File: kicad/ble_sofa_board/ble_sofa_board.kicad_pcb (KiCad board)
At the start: 2 copper layers, 21 parts, among them J1 Screw_Terminal_01x02 VIN, J2 Screw_Terminal_01x02 VOUT, J3 Conn_01x04, J5 Screw_Terminal_01x02 RelayUp, J6 Screw_Terminal_01x02 RelayDwn, J7 RJ9, U1 LM2596S_Buck_Module, U3 Pico_Dual_Channel_Relay_HAT

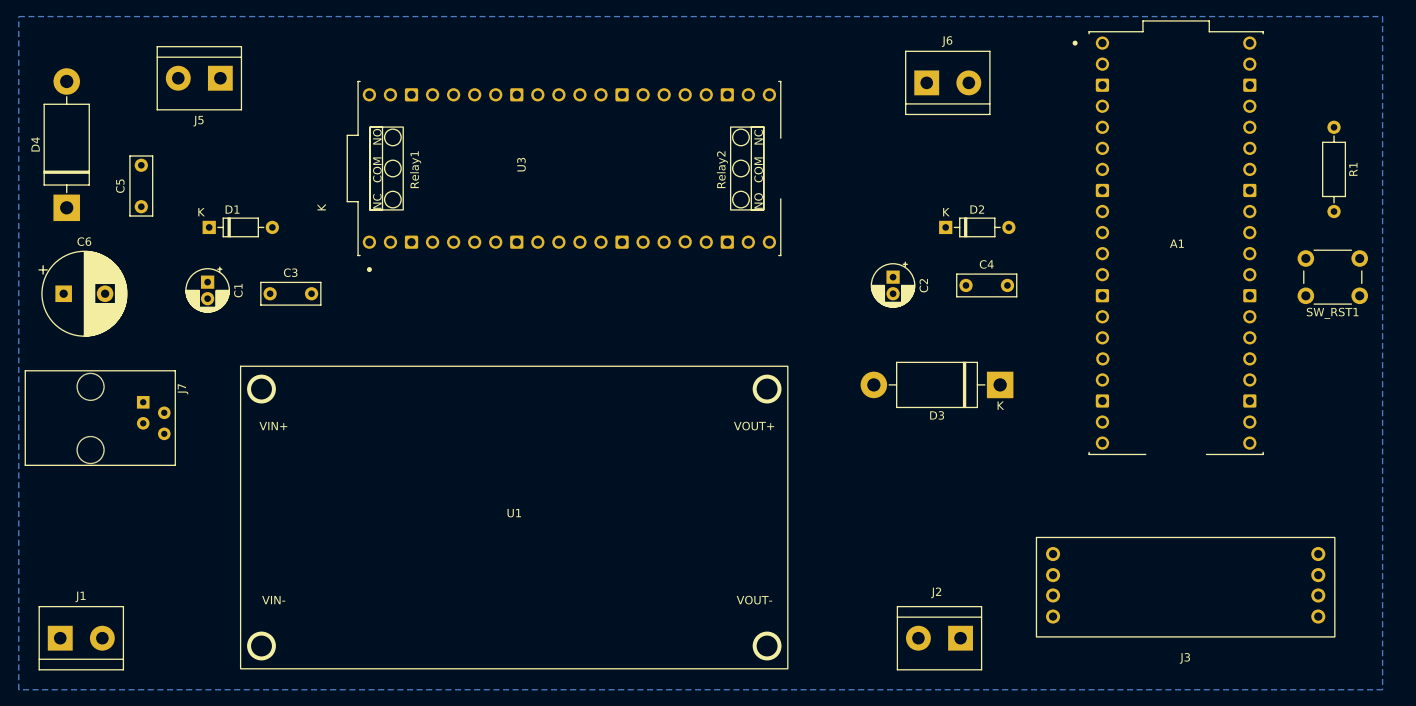
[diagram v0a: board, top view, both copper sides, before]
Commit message: ble_sofa - pcb - WIP routing
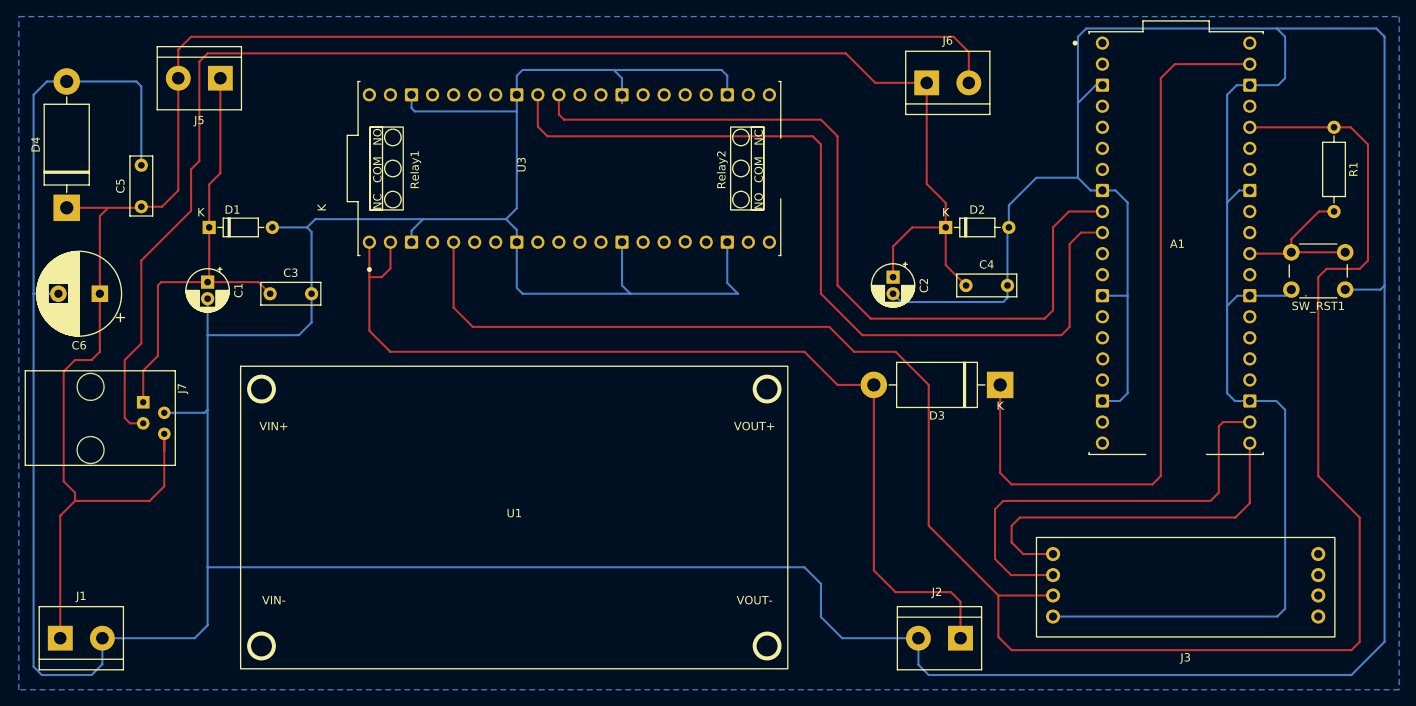
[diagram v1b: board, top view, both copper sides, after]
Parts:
- moved C6 4.37 mm to (67.0, 69.0), turned to 180 degrees
- moved SW_RST1 1.90 mm to (217.2, 68.5)
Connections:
- A1 pad 10: RELAY2_PIN -> RELAY1_PIN
- A1 pad 9: RELAY1_PIN -> RELAY2_PIN
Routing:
- net GND: track 0.00 -> 821.6 mm
- net +3.3V: track 0.00 -> 236.3 mm
- net VCC: track 0.00 -> 208.9 mm
- net RJ9_DWN: track 0.00 -> 176.3 mm
- net Net-(D3-A): track 0.00 -> 119.2 mm
- net RELAY1_PIN: track 0.00 -> 103.9 mm
- net RELAY2_PIN: track 0.00 -> 99.9 mm
- net Net-(A1-VSYS): track 0.00 -> 90.4 mm
- net RJ9_UP: track 0.00 -> 54.6 mm
- net OLED_SCL: track 0.00 -> 53.6 mm
- net OLED_SDA: track 0.00 -> 44.7 mm
- net Net-(A1-RUN): track 0.00 -> 19.7 mm

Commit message: ble_sofa - pcb - Complete routing
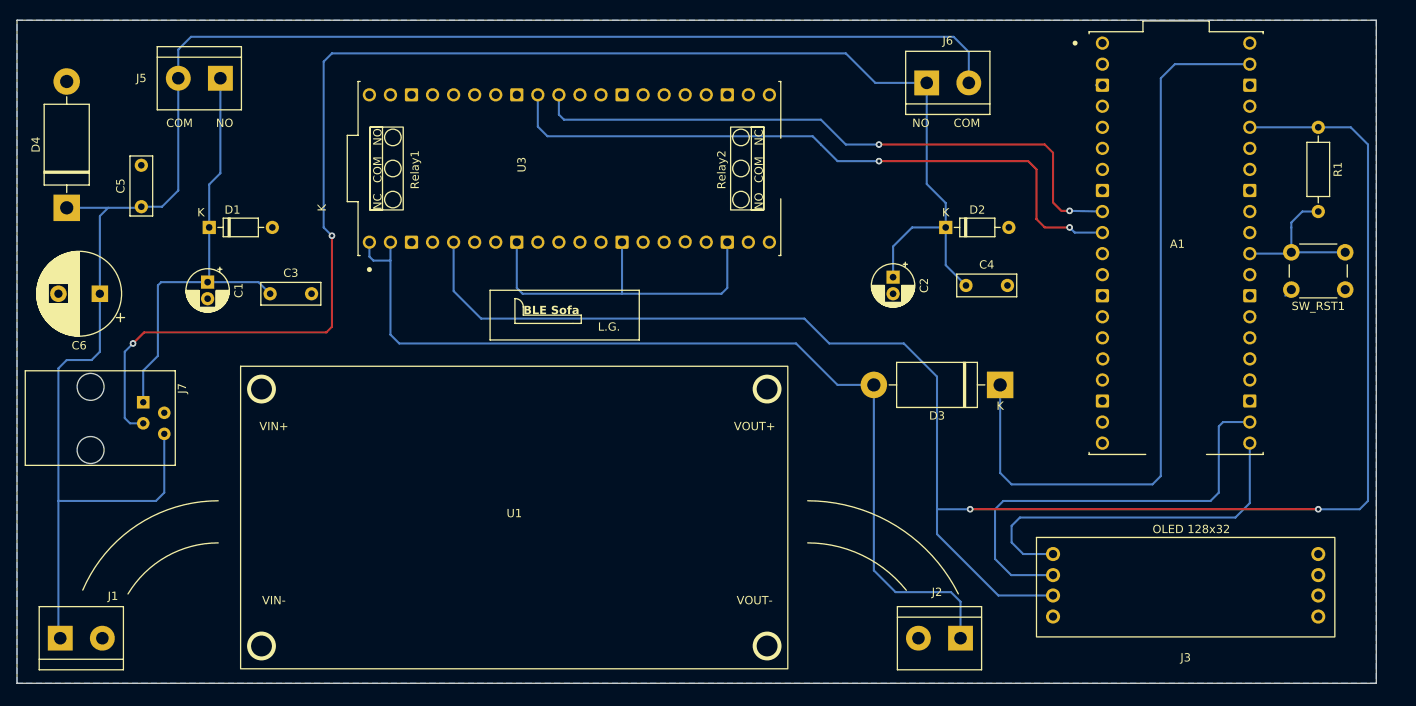
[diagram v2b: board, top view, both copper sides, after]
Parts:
- moved R1 1.90 mm to (214.0, 48.9)
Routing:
- net GND: track 821.6 -> 45.6 mm
- net RELAY2_PIN: track 99.9 -> 76.4 mm, vias 0 -> 2
- net RELAY1_PIN: track 103.9 -> 80.8 mm, vias 0 -> 2
- net +3.3V: track 236.3 -> 215.1 mm, vias 0 -> 2
- net RJ9_DWN: track 176.3 -> 181.2 mm, vias 0 -> 2
- net Net-(D3-A): track 119.2 -> 115.3 mm
- net Net-(A1-RUN): track 19.7 -> 19.0 mm
- added copper zone on B.Cu, net GND
- removed copper zone on B.Cu, net (none)
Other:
- board outline added: 164 x 80 mm
- board text added: "BLE Sofa"
- board text added: "COM"
- board text added: "L.G."
- board text added: "NO"
- board text added: "OLED 128x32"

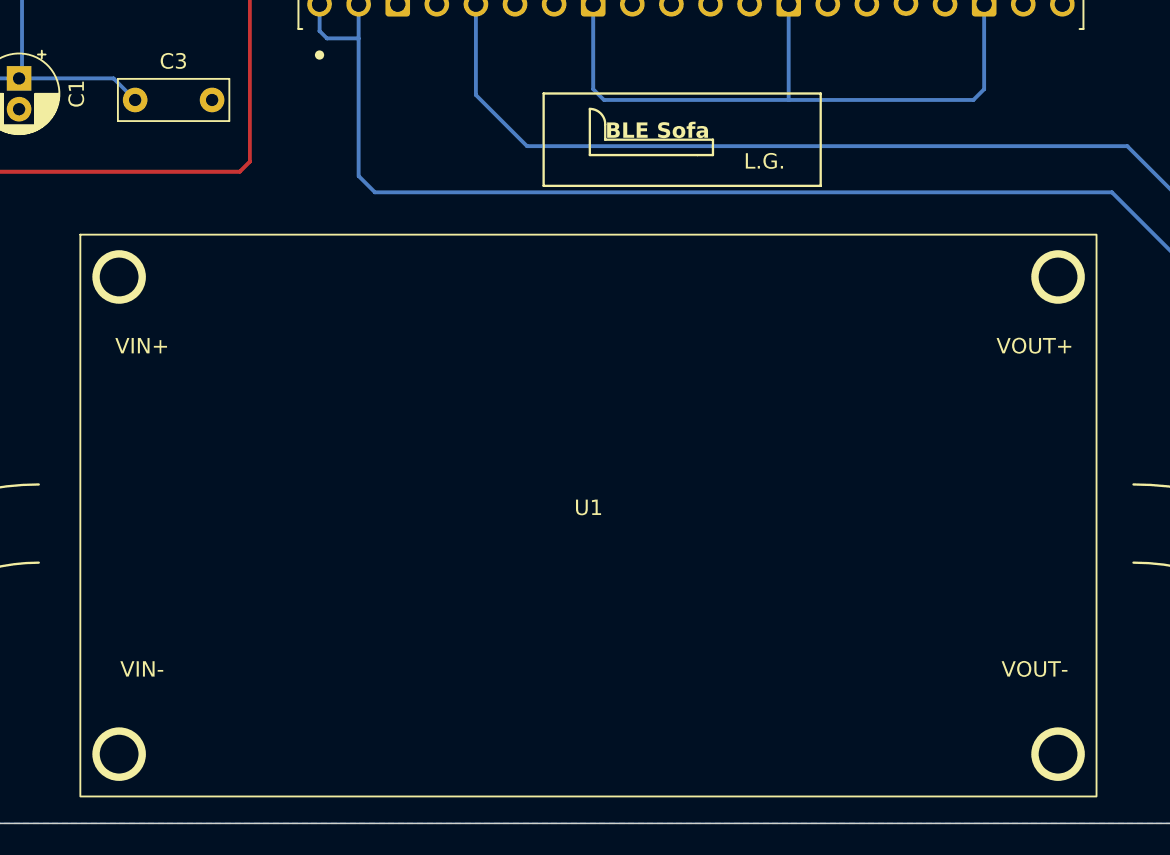
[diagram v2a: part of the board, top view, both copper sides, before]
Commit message: ble_sofa - pcb - Minor update + Gerber files generation
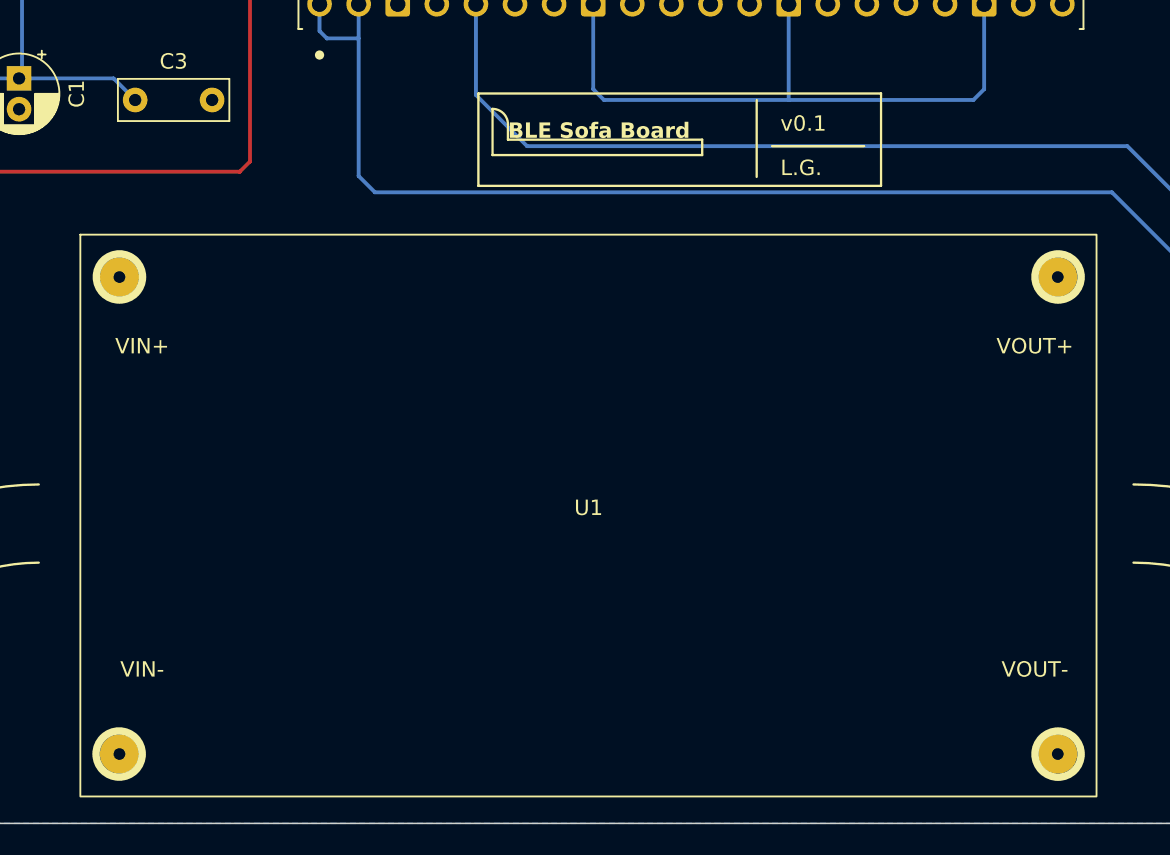
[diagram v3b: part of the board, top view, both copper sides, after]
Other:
- board text added: "BLE Sofa Board"
- board text added: "v0.1"
- board text removed: "BLE Sofa"
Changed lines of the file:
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@@
   )
   (paper "A4")
+  (title_block
+    (title "BLE Sofa Board")
+    (date "2024-03-17")
+    (rev "0.1")
+  )
   (layers
     (0 "F.Cu" signal)
@@
       (viasonmask false)
       (mode 1)
-      (useauxorigin false)
+      (useauxorigin true)
       (hpglpennumber 1)
       (hpglpenspeed 20)
@@
       (plotinvisibletext false)
       (sketchpadsonfab false)
-      (subtractmaskfromsilk false)
+      (subtractmaskfromsilk true)
       (outputformat 1)
       (mirror false)
-      (drillshape 1)
+      (drillshape 0)
       (scaleselection 1)
-      (outputdirectory "")
+      (outputdirectory "export/20240317/gerber/01/")
     )
   )
@@
         (effects (font (size 1 1) (thickness 0.15)))
     )
+    (fp_text user "VOUT-" (at 29 10 unlocked) (layer "F.SilkS")
+        (effects (font (size 1 1) (thickness 0.15)))
+    )
     (fp_text user "VOUT+" (at 29 -11 unlocked) (layer "F.SilkS")
         (effects (font (size 1 1) (thickness 0.15)))
     )
+    (fp_text user "VIN-" (at -29 10 unlocked) (layer "F.SilkS")
+        (effects (font (size 1 1) (thickness 0.15)))
+    )
     (fp_text user "VIN+" (at -29 -11 unlocked) (layer "F.SilkS")
-        (effects (font (size 1 1) (thickness 0.15)))
-    )
-    (fp_text user "VOUT-" (at 29 10 unlocked) (layer "F.SilkS")
-        (effects (font (size 1 1) (thickness 0.15)))
-    )
-    (fp_text user "VIN-" (at -29 10 unlocked) (layer "F.SilkS")
         (effects (font (size 1 1) (thickness 0.15)))
     )
@@
     (fp_rect (start -33.02 -18.25) (end 33 18.25)
       (stroke (width 0.12) (type solid)) (fill none) (layer "F.SilkS"))
-    (fp_circle (center -30.5 -15.5) (end -29 -15.5)
+    (fp_circle (center -30.5 15.494) (end -29 15.494)
       (stroke (width 0.48) (type solid)) (fill none) (layer "F.SilkS"))
-    (fp_circle (center -30.5 15.5) (end -29 15.5)
+    (fp_circle (center -30.48 -15.5) (end -28.98 -15.5)
       (stroke (width 0.48) (type solid)) (fill none) (layer "F.SilkS"))
     (fp_circle (center 30.5 -15.5) (end 32 -15.5)
@@
     (fp_circle (center 30.5 15.5) (end 32 15.5)
       (stroke (width 0.48) (type solid)) (fill none) (layer "F.SilkS"))
+    (pad "1" thru_hole circle (at -30.48 -15.494) (size 2.54 2.54) (drill 0.762) (layers "*.Cu" "*.Mask"))
+    (pad "2" thru_hole circle (at 30.48 -15.494) (size 2.54 2.54) (drill 0.762) (layers "*.Cu" "*.Mask"))
+    (pad "3" thru_hole circle (at 30.48 15.494) (size 2.54 2.54) (drill 0.762) (layers "*.Cu" "*.Mask"))
+    (pad "4" thru_hole circle (at -30.48 15.494) (size 2.54 2.54) (drill 0.762) (layers "*.Cu" "*.Mask"))
     (model "/home/laurent/Projects/lgantel/ble_sofa/kicad/3d_models/lm2596-buck-converter/LM2596 Buck Converter 4.0-40 to 1.3-37V.STEP"
       (offset (xyz 0.1 0 0))
@@
   (gr_arc (start 70.38984 105.225904) (mid 75.022725 100.708461) (end 81.28 99.06)
     (stroke (width 0.15) (type default)) (layer "F.SilkS"))
+  (gr_line (start 127.92 74) (end 127.92 69)
+    (stroke (width 0.15) (type default)) (layer "F.SilkS"))
+  (gr_line (start 128.92 72) (end 134.92 72)
+    (stroke (width 0.15) (type default)) (layer "F.SilkS"))
   (gr_arc (start 152.4 99.06) (mid 159.001796 100.564139) (end 164.300441 104.779647)
     (stroke (width 0.15) (type default)) (layer "F.SilkS"))
-  (gr_line (start 117.08 69.58) (end 117.08 72.58)
+  (gr_line (start 110.76 69.58) (end 110.76 72.58)
     (stroke (width 0.15) (type default)) (layer "F.SilkS"))
   (gr_arc (start 152.4 93.98) (mid 163.082856 97.014776) (end 170.574761 105.21262)
     (stroke (width 0.15) (type default)) (layer "F.SilkS"))
-  (gr_line (start 118.08 70.58) (end 118.08 71.58)
+  (gr_line (start 111.76 70.58) (end 111.76 71.58)
     (stroke (width 0.15) (type default)) (layer "F.SilkS"))
-  (gr_line (start 125.08 72.58) (end 125.08 71.58)
+  (gr_line (start 124.38 72.58) (end 124.38 71.58)
     (stroke (width 0.15) (type default)) (layer "F.SilkS"))
-  (gr_rect (start 114.08 68.58) (end 132.08 74.58)
+  (gr_rect (start 109.84 68.58) (end 136 74.58)
     (stroke (width 0.15) (type default)) (fill none) (layer "F.SilkS"))
-  (gr_arc (start 117.08 69.58) (mid 117.787107 69.872893) (end 118.08 70.58)
+  (gr_arc (start 110.76 69.58) (mid 111.467107 69.872893) (end 111.76 70.58)
     (stroke (width 0.15) (type default)) (layer "F.SilkS"))
-  (gr_line (start 118.08 71.58) (end 125.08 71.58)
+  (gr_line (start 111.76 71.58) (end 124.38 71.58)
     (stroke (width 0.15) (type default)) (layer "F.SilkS"))
-  (gr_line (start 124.08 72.58) (end 125.08 72.58)
-    (stroke (width 0.15) (type default)) (layer "F.SilkS"))
-  (gr_line (start 117.08 72.58) (end 124.08 72.58)
+  (gr_line (start 110.76 72.58) (end 124.38 72.58)
     (stroke (width 0.15) (type default)) (layer "F.SilkS"))
   (gr_arc (start 64.937601 104.756115) (mid 71.49227 96.916525) (end 81.28 93.98)
@@
   (gr_rect (start 57 36) (end 221 116)
     (stroke (width 0.1) (type default)) (fill none) (layer "Edge.Cuts"))
-  (gr_text "L.G." (at 127.08 73.58) (layer "F.SilkS")
+  (gr_text "v0.1" (at 129.46 71.12) (layer "F.SilkS")
+    (effects (font (size 1 1) (thickness 0.15)) (justify left bottom))
+  )
+  (gr_text "L.G." (at 129.46 74) (layer "F.SilkS")
     (effects (font (size 1 1) (thickness 0.15)) (justify left bottom))
   )
@@
     (effects (font (size 1 1) (thickness 0.15)) (justify left bottom))
   )
-  (gr_text "BLE Sofa" (at 118.08 71.58) (layer "F.SilkS")
+  (gr_text "BLE Sofa Board" (at 111.76 71.58) (layer "F.SilkS")
     (effects (font (size 1 1) (thickness 0.2) bold) (justify left bottom))
   )

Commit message: ble_sofa - pcb - Update Gerber files
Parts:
- moved C4 3.86 mm to (167.6, 68.0)
- moved D2 3.86 mm to (165.2, 61.0)
- moved C2 3.86 mm to (158.8, 67.0)
- moved A1 3.81 mm to (193.0, 62.9)
- moved R1 3.81 mm to (210.2, 48.9)
- moved SW_RST1 3.81 mm to (213.4, 68.5)
- moved J3 2.42 mm to (195.6, 113.4)
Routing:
- net +3.3V: track 215.1 -> 186.5 mm, vias 2 -> 0
- net OLED_SDA: track 44.7 -> 34.2 mm
- net OLED_SCL: track 53.6 -> 43.1 mm
- net RELAY1_PIN: track 80.8 -> 73.6 mm
- net Net-(A1-VSYS): track 90.4 -> 84.0 mm
- net RELAY2_PIN: track 76.4 -> 71.4 mm
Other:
- board size 164 x 80 mm -> 160 x 80 mm
